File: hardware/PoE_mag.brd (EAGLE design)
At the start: 149.9 x 124.5 mm, 129 parts, among them IC1 LD1117V33, IC10 74LVC1T45SOT23-HAND, IC11 74LVC1T45SOT23-HAND, IC12 PCA9517A, IC2 LD1117V33, IC3 DS1338, IC4 ATMEGA1284, IC5 TSR 1-2450, IC6 LM61, IC7 MCP2200, IC8 74LVC1T45SOT23-HAND, IC9 74LVC1T45SOT23-HAND, Q1 BSS138, Q2 BUK98150-55A, X1 PWR, X2 JTAG, X3 USB, X4 MICRO-SD-SOCKETHIROSE-DM3D, X5 CONN-SMATHD, X6 UFL, X7 22-23-2021, X8 RJ45, X9 RJ11, Y1 32k768, Y2 12MHz, Y3 12MHz

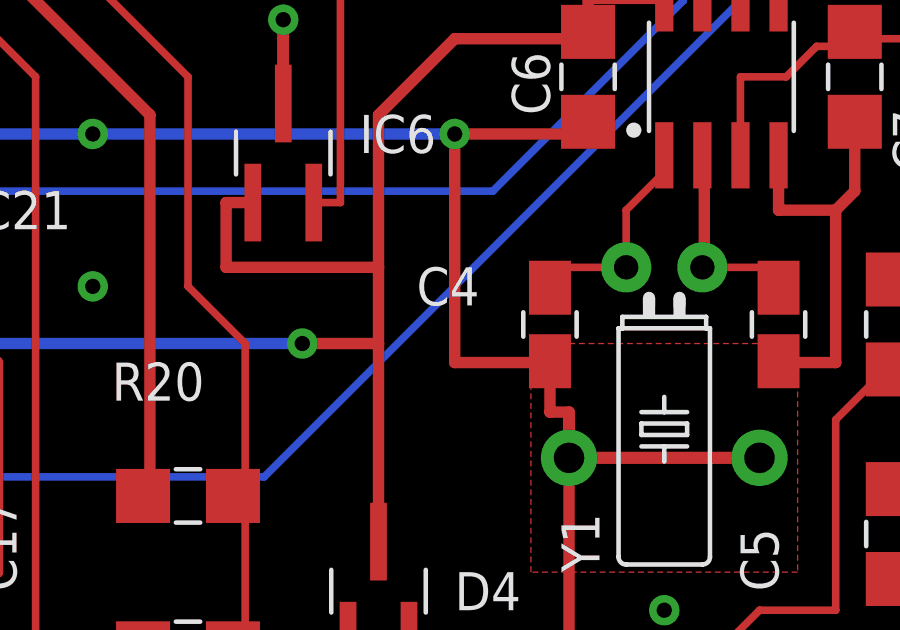
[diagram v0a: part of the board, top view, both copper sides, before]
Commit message: Show alternative build configurations more clearly
Move TO-220 variant of LD1117V33 to show it is the alternative
fit. Use short dashed lines to connect all optional/variant
components. Add "*" suffix to component values which are
optional/variants to ease construction o the standard version. Minor
silkscreen changes on board to accomodate longer text.
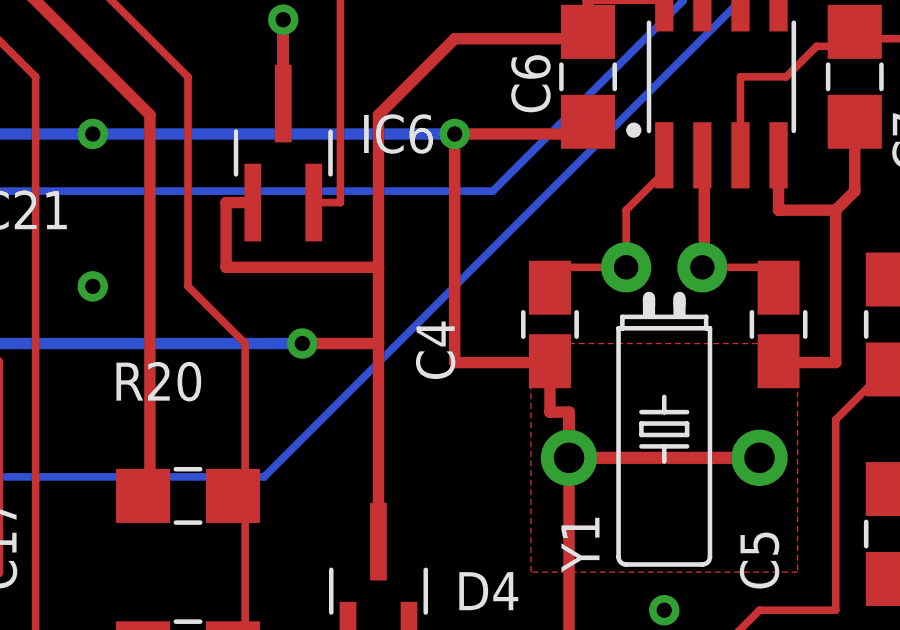
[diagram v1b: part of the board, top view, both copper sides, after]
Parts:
- C2: value 1u -> 1u*
- C4, C5: value 15p -> 15p*
- C7: value 100p -> 100p*
- D2: value BAS40 -> BAS40*
- IC2: value LD1117V33 -> LD1117V33*
- R9: value 1k -> 1k*
- X8: value RJ45 -> RJ45*
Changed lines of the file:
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@@
 <wire x1="144.145" y1="24.13" x2="142.875" y2="24.765" width="0.254" layer="27"/>
 <wire x1="143.51" y1="23.495" x2="144.145" y2="24.13" width="0.254" layer="27"/>
-<wire x1="144.145" y1="23.495" x2="144.145" y2="22.225" width="0.254" layer="27"/>
+<wire x1="144.145" y1="23.495" x2="144.145" y2="22.86" width="0.254" layer="27"/>
 <rectangle x1="24.384" y1="87.376" x2="27.94" y2="88.9" layer="41"/>
 <rectangle x1="30.48" y1="87.376" x2="32.766" y2="88.9" layer="41"/>
@@
 <attribute name="VALUE" x="134.62" y="59.055" size="1.27" layer="27" ratio="10" rot="R90"/>
 </element>
-<element name="C2" library="SteveMarple" package="1206-HAND" value="1u" x="62.865" y="24.765" smashed="yes" rot="R180">
+<element name="C2" library="SteveMarple" package="1206-HAND" value="1u*" x="62.865" y="24.765" smashed="yes" rot="R180">
 <attribute name="NAME" x="66.04" y="25.7175" size="1.27" layer="25" ratio="10"/>
 <attribute name="VALUE" x="66.04" y="23.8125" size="1.27" layer="27" ratio="10"/>
@@
 <attribute name="VALUE" x="127.635" y="78.105" size="1.27" layer="27" ratio="10" rot="SR90"/>
 </element>
-<element name="D2" library="SteveMarple" package="SOT23-3-HAND" value="BAS40" x="142.875" y="15.24" smashed="yes" rot="R180">
+<element name="D2" library="SteveMarple" package="SOT23-3-HAND" value="BAS40*" x="142.875" y="15.24" smashed="yes" rot="R180">
 <attribute name="NAME" x="142.24" y="11.684" size="1.27" layer="25" ratio="10" rot="SR0"/>
 <attribute name="VALUE" x="142.24" y="10.795" size="1.016" layer="27" ratio="10" rot="SR0" align="top-left"/>
 </element>
-<element name="C7" library="SteveMarple" package="1206-HAND" value="100p" x="145.415" y="35.56" smashed="yes" rot="R270">
+<element name="C7" library="SteveMarple" package="1206-HAND" value="100p*" x="145.415" y="35.56" smashed="yes" rot="R270">
 <attribute name="NAME" x="147.955" y="32.385" size="1.27" layer="25" ratio="10" rot="R90"/>
-<attribute name="VALUE" x="147.955" y="36.195" size="1.27" layer="27" ratio="10" rot="R90"/>
-</element>
-<element name="R9" library="SteveMarple" package="1206-HAND" value="1k" x="146.685" y="27.305" smashed="yes" rot="R90">
+<attribute name="VALUE" x="147.955" y="35.56" size="1.27" layer="27" ratio="10" rot="R90"/>
+</element>
+<element name="R9" library="SteveMarple" package="1206-HAND" value="1k*" x="146.685" y="27.305" smashed="yes" rot="R90">
 <attribute name="NAME" x="149.225" y="24.765" size="1.27" layer="25" ratio="10" rot="R90"/>
 <attribute name="VALUE" x="149.225" y="27.94" size="1.27" layer="27" ratio="10" rot="R90"/>
@@
 <attribute name="VALUE" x="107.315" y="27.94" size="1.27" layer="27" ratio="10"/>
 </element>
-<element name="C5" library="SteveMarple" package="0805-HAND" value="15p" x="142.875" y="27.305" smashed="yes" rot="R270">
+<element name="C5" library="SteveMarple" package="0805-HAND" value="15p*" x="142.875" y="27.305" smashed="yes" rot="R270">
 <attribute name="NAME" x="142.875" y="18.415" size="1.27" layer="25" ratio="10" rot="R90"/>
 <attribute name="VALUE" x="144.78" y="18.415" size="1.27" layer="27" ratio="10" rot="R90"/>
 </element>
-<element name="C4" library="SteveMarple" package="0805-HAND" value="15p" x="135.255" y="27.305" smashed="yes" rot="R270">
-<attribute name="NAME" x="130.81" y="27.94" size="1.27" layer="25" ratio="10"/>
-<attribute name="VALUE" x="130.81" y="26.035" size="1.27" layer="27" ratio="10"/>
+<element name="C4" library="SteveMarple" package="0805-HAND" value="15p*" x="135.255" y="27.305" smashed="yes" rot="R270">
+<attribute name="NAME" x="132.08" y="25.4" size="1.27" layer="25" ratio="10" rot="R90"/>
+<attribute name="VALUE" x="133.858" y="25.4" size="1.27" layer="27" ratio="10" rot="R90"/>
 </element>
 <element name="R3" library="SteveMarple" package="1206-HAND" value="1M" x="64.77" y="96.52" smashed="yes">
@@
 <attribute name="VALUE" x="83.82" y="20.955" size="1.27" layer="27" ratio="10" align="bottom-center"/>
 </element>
-<element name="IC2" library="SteveMarple" package="TO220" value="LD1117V33" x="63.5" y="17.78" smashed="yes" rot="R90">
+<element name="IC2" library="SteveMarple" package="TO220" value="LD1117V33*" x="63.5" y="17.78" smashed="yes" rot="R90">
 <attribute name="NAME" x="57.785" y="15.24" size="1.27" layer="25" ratio="10" rot="R90"/>
 <attribute name="VALUE" x="58.42" y="12.7" size="1.27" layer="27" ratio="10" rot="R90" align="top-left"/>
@@
 <attribute name="NAME" x="40.64" y="46.99" size="1.27" layer="25" ratio="10" rot="R90"/>
 </element>
-<element name="X8" library="SteveMarple" package="RJ45-8" value="RJ45" x="11.43" y="69.215" smashed="yes" rot="R90">
+<element name="X8" library="SteveMarple" package="RJ45-8" value="RJ45*" x="11.43" y="69.215" smashed="yes" rot="R90">
 <attribute name="NAME" x="10.795" y="77.47" size="1.27" layer="25" ratio="10" rot="R90"/>
 <attribute name="VALUE" x="12.7" y="77.47" size="1.27" layer="27" ratio="10" rot="R90"/>

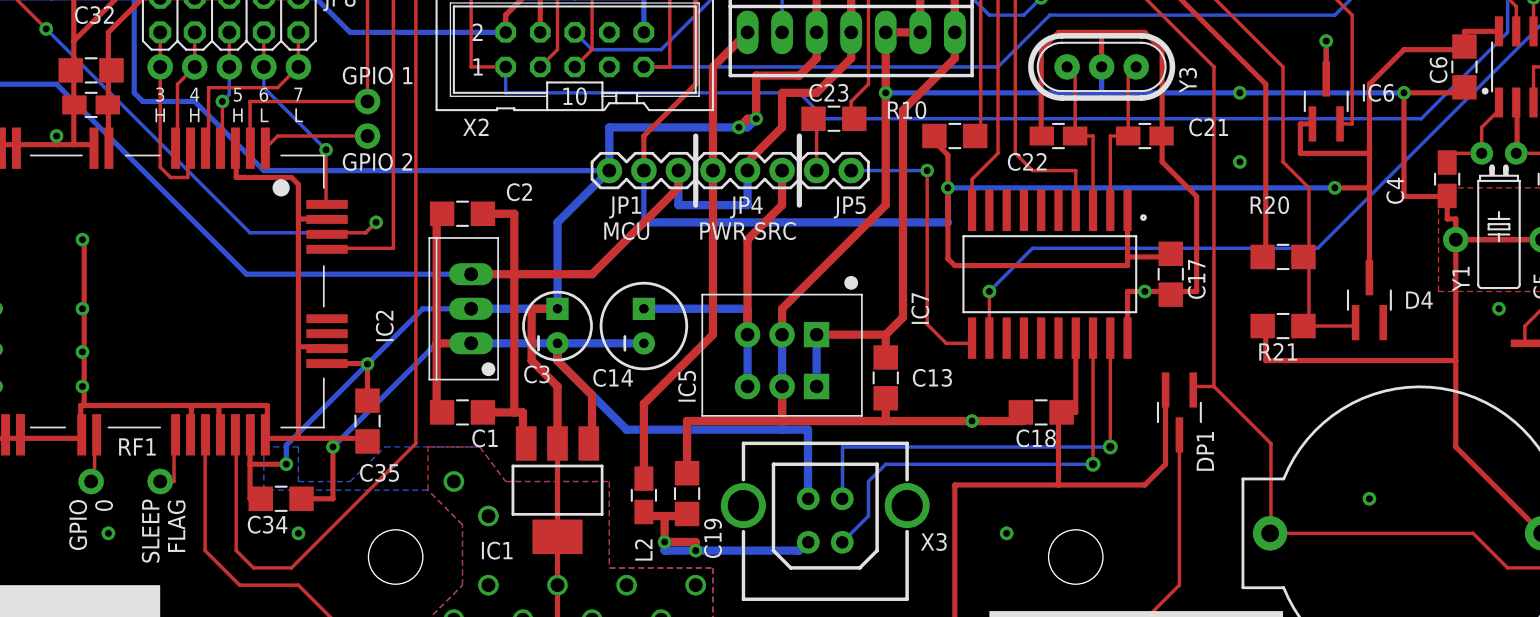
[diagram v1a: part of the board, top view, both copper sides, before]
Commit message: Add decoupling for supply voltage measurement
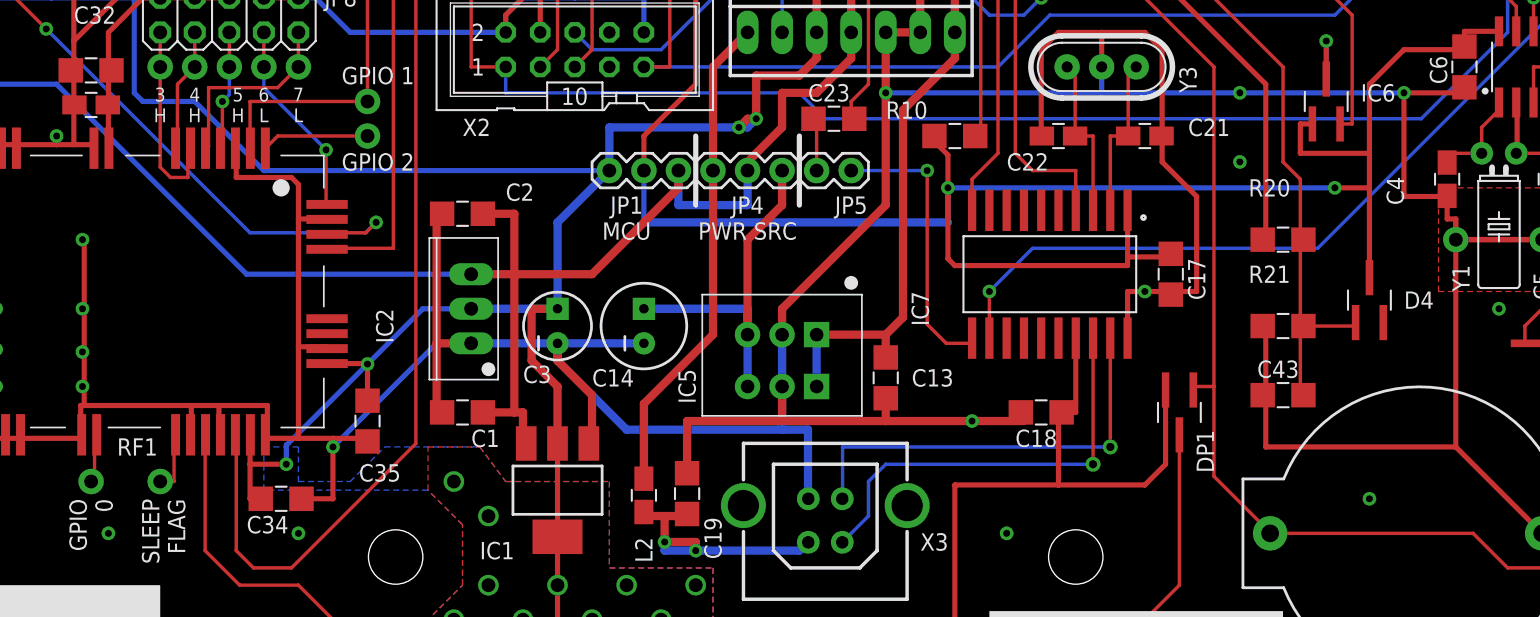
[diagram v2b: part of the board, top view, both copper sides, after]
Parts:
- added C43: 100n, SteveMarple:1206-HAND
- moved R20 1.27 mm to (123.2, 22.9)
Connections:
- net A2: now also C43.1
- net GND: now also C43.2
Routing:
- net GND: track 1232.4 -> 1239.0 mm
- net A2: track 66.1 -> 71.6 mm
- net VIN: track 279.1 -> 277.8 mm
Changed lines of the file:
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@@
 <attribute name="VALUE" x="28.575" y="75.565" size="1.27" layer="27" ratio="10"/>
 </element>
-<element name="R20" library="SteveMarple" package="1206-HAND" value="3k 1%" x="123.19" y="21.59" smashed="yes">
-<attribute name="NAME" x="120.65" y="24.765" size="1.27" layer="25" ratio="10"/>
-<attribute name="VALUE" x="120.65" y="22.86" size="1.27" layer="27" ratio="10"/>
+<element name="R20" library="SteveMarple" package="1206-HAND" value="3k 1%" x="123.19" y="22.86" smashed="yes">
+<attribute name="NAME" x="120.65" y="26.035" size="1.27" layer="25" ratio="10"/>
+<attribute name="VALUE" x="120.65" y="24.13" size="1.27" layer="27" ratio="10"/>
 </element>
 <element name="R21" library="SteveMarple" package="1206-HAND" value="1k 1%" x="123.19" y="16.51" smashed="yes">
-<attribute name="NAME" x="121.285" y="13.97" size="1.27" layer="25" ratio="10"/>
-<attribute name="VALUE" x="121.285" y="12.065" size="1.27" layer="27" ratio="10"/>
+<attribute name="NAME" x="120.65" y="19.685" size="1.27" layer="25" ratio="10"/>
+<attribute name="VALUE" x="120.65" y="17.78" size="1.27" layer="27" ratio="10"/>
 </element>
 <element name="D4" library="SteveMarple" package="SOT23-3-HAND" value="BAS40" x="129.54" y="18.415" smashed="yes" rot="R90">
@@
 <attribute name="NAME" x="39.37" y="85.09" size="1.27" layer="25" ratio="10" rot="R90"/>
 <attribute name="VALUE" x="41.275" y="85.09" size="1.27" layer="27" ratio="10" rot="R90"/>
+</element>
+<element name="C43" library="SteveMarple" package="1206-HAND" value="100n" x="123.19" y="11.43" smashed="yes" rot="R180">
+<attribute name="NAME" x="121.285" y="12.7" size="1.27" layer="25" ratio="10"/>
 </element>
 </elements>
@@
 <wire x1="50.8" y1="8.255" x2="50.8" y2="14.986" width="0.381" layer="1"/>
 <wire x1="34.798" y1="10.668" x2="34.798" y2="8.636" width="0.381" layer="1"/>
-<wire x1="42.926" y1="10.668" x2="40.64" y2="10.668" width="0.381" layer="1"/>
-<wire x1="37.084" y1="10.668" x2="40.64" y2="10.668" width="0.381" layer="1"/>
-<wire x1="37.084" y1="10.668" x2="35.052" y2="10.668" width="0.381" layer="1"/>
+<wire x1="35.052" y1="10.668" x2="42.926" y2="10.668" width="0.381" layer="1"/>
 <wire x1="35.052" y1="10.668" x2="34.798" y2="10.668" width="0.381" layer="1"/>
 <wire x1="34.798" y1="8.636" x2="34.87" y2="8.515" width="0.381" layer="1"/>
@@
 <wire x1="114.3" y1="30.48" x2="114.255" y2="30.48" width="0.381" layer="1"/>
 <wire x1="121.92" y1="16.51" x2="121.793" y2="16.637" width="0.381" layer="1"/>
-<wire x1="121.92" y1="13.97" x2="121.92" y2="16.51" width="0.381" layer="1"/>
-<wire x1="135.89" y1="13.97" x2="121.92" y2="13.97" width="0.381" layer="1"/>
-<wire x1="135.89" y1="22.86" x2="135.89" y2="13.97" width="0.381" layer="1"/>
+<wire x1="121.92" y1="7.62" x2="121.92" y2="11.43" width="0.381" layer="1"/>
+<wire x1="121.92" y1="11.43" x2="121.92" y2="16.51" width="0.381" layer="1"/>
+<wire x1="135.89" y1="7.62" x2="121.92" y2="7.62" width="0.381" layer="1"/>
+<wire x1="135.89" y1="22.86" x2="135.89" y2="7.62" width="0.381" layer="1"/>
 <wire x1="121.92" y1="16.51" x2="121.691" y2="16.51" width="0.381" layer="1"/>
 <wire x1="132.08" y1="33.655" x2="136.525" y2="33.655" width="0.381" layer="1"/>
@@
 <wire x1="143.002" y1="26.162" x2="142.875" y2="26.08" width="0.381" layer="1"/>
 <wire x1="135.89" y1="7.62" x2="142.24" y2="1.27" width="0.381" layer="1"/>
-<wire x1="135.89" y1="13.97" x2="135.89" y2="7.62" width="0.381" layer="1"/>
 <wire x1="132.08" y1="33.655" x2="126.365" y2="33.655" width="0.381" layer="16"/>
 <wire x1="60.96" y1="24.765" x2="61.366" y2="24.765" width="0.6096" layer="1"/>
@@
 <wire x1="142.24" y1="22.86" x2="135.89" y2="22.86" width="0.4064" layer="1"/>
 <wire x1="135.89" y1="22.86" x2="135.89" y2="24.384" width="0.4064" layer="1"/>
+<contactref element="C43" pad="2"/>
+<wire x1="121.691" y1="11.43" x2="121.92" y2="11.43" width="0.381" layer="1"/>
 </signal>
 <signal name="VCC" class="1">
@@
 <contactref element="R8" pad="1"/>
 <contactref element="DP1" pad="1"/>
-<wire x1="122.301" y1="7.874" x2="118.11" y2="12.065" width="0.254" layer="1"/>
+<wire x1="118.11" y1="5.461" x2="118.11" y2="12.065" width="0.254" layer="1"/>
 <wire x1="118.11" y1="12.065" x2="116.586" y2="12.065" width="0.254" layer="1"/>
-<wire x1="122.301" y1="1.27" x2="122.301" y2="7.874" width="0.254" layer="1"/>
+<wire x1="122.301" y1="1.27" x2="118.11" y2="5.461" width="0.254" layer="1"/>
 <wire x1="116.586" y1="12.065" x2="116.586" y2="11.811" width="0.254" layer="1"/>
 <wire x1="86.36" y1="40.64" x2="86.36" y2="38.1" width="0.254" layer="16"/>
@@
 <wire x1="109.22" y1="46.355" x2="93.98" y2="61.595" width="0.254" layer="1"/>
 <wire x1="93.98" y1="61.595" x2="93.98" y2="62.23" width="0.254" layer="1"/>
-<wire x1="128.524" y1="16.51" x2="125.095" y2="16.51" width="0.254" layer="1"/>
+<wire x1="128.524" y1="16.51" x2="124.689" y2="16.51" width="0.254" layer="1"/>
 <wire x1="128.524" y1="16.764" x2="128.524" y2="16.51" width="0.254" layer="1"/>
-<wire x1="125.095" y1="16.51" x2="125.095" y2="21.59" width="0.254" layer="1"/>
-<wire x1="125.095" y1="16.51" x2="124.689" y2="16.51" width="0.254" layer="1"/>
+<wire x1="124.46" y1="16.51" x2="124.46" y2="22.86" width="0.254" layer="1"/>
 <wire x1="115.57" y1="43.18" x2="123.19" y2="35.56" width="0.254" layer="1"/>
 <wire x1="123.19" y1="35.56" x2="123.19" y2="28.575" width="0.254" layer="1"/>
-<wire x1="123.19" y1="28.575" x2="125.095" y2="26.67" width="0.254" layer="1"/>
-<wire x1="125.095" y1="26.67" x2="125.095" y2="21.59" width="0.254" layer="1"/>
+<wire x1="123.19" y1="28.575" x2="124.46" y2="27.305" width="0.254" layer="1"/>
+<wire x1="124.46" y1="27.305" x2="124.46" y2="22.86" width="0.254" layer="1"/>
+<wire x1="124.46" y1="22.86" x2="124.689" y2="22.86" width="0.254" layer="1"/>
 <wire x1="109.22" y1="44.45" x2="110.49" y2="43.18" width="0.254" layer="1"/>
 <wire x1="110.49" y1="43.18" x2="115.57" y2="43.18" width="0.254" layer="1"/>
 <wire x1="109.22" y1="45.72" x2="109.22" y2="44.45" width="0.254" layer="1"/>
-<wire x1="125.095" y1="21.59" x2="124.689" y2="21.59" width="0.254" layer="1"/>
+<wire x1="125.095" y1="22.86" x2="124.689" y2="22.86" width="0.254" layer="1"/>
+<contactref element="C43" pad="1"/>
+<wire x1="124.689" y1="11.43" x2="124.46" y2="11.43" width="0.254" layer="1"/>
+<wire x1="124.46" y1="11.43" x2="124.46" y2="16.51" width="0.254" layer="1"/>
+<wire x1="124.46" y1="16.51" x2="124.689" y2="16.51" width="0.254" layer="1"/>
 </signal>
 <signal name="A3">
@@
 <wire x1="93.98" y1="15.875" x2="93.98" y2="14.199" width="0.6096" layer="1"/>
 <wire x1="93.98" y1="13.97" x2="93.98" y2="14.199" width="0.6096" layer="1"/>
-<wire x1="121.92" y1="21.59" x2="121.691" y2="21.59" width="0.381" layer="1"/>
-<wire x1="121.92" y1="34.29" x2="121.92" y2="21.59" width="0.381" layer="1"/>
+<wire x1="121.92" y1="34.29" x2="121.92" y2="22.86" width="0.381" layer="1"/>
 <wire x1="114.3" y1="41.91" x2="121.92" y2="34.29" width="0.381" layer="1"/>
 <wire x1="99.06" y1="45.72" x2="101.092" y2="45.72" width="0.381" layer="1"/>
@@
 <wire x1="106.68" y1="43.18" x2="107.95" y2="41.91" width="0.381" layer="1"/>
 <wire x1="107.95" y1="41.91" x2="114.3" y2="41.91" width="0.381" layer="1"/>
-<wire x1="121.666" y1="21.59" x2="121.691" y2="21.59" width="0.381" layer="1"/>
+<wire x1="121.92" y1="22.86" x2="121.691" y2="22.86" width="0.381" layer="1"/>
 <wire x1="99.06" y1="45.72" x2="99.06" y2="38.1" width="0.6096" layer="1"/>
 <wire x1="95.25" y1="17.145" x2="93.98" y2="15.875" width="0.6096" layer="1"/>
